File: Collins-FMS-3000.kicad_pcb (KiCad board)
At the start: 2 copper layers, 145 x 161 mm, 142 parts, among them J1 USB_B_Mini, J2 AVR-ISP-6, J3 Conn_02x04_Odd_Even, SW1 SW_Push_LED, SW10 SW_Push_LED, SW11 SW_Push_LED, SW12 SW_Push_LED, SW13 SW_Push_LED, SW14 SW_Push_LED, SW15 SW_Push_LED, SW16 SW_Push_LED, SW17 SW_Push_LED, SW18 SW_Push_LED, SW19 SW_Push_LED, SW2 SW_Push_LED, SW20 SW_Push_LED, SW21 SW_Push_LED, SW22 SW_Push_LED, SW23 SW_Push_LED, SW24 SW_Push_LED, SW25 SW_Push_LED, SW26 SW_Push_LED, SW27 SW_Push_LED, SW28 SW_Push_LED, SW29 SW_Push_LED, SW3 SW_Push_LED, SW30 SW_Push_LED, SW31 SW_Push_LED, SW32 SW_Push_LED, SW33 SW_Push_LED, SW34 SW_Push_LED, SW35 SW_Push_LED, SW36 SW_Push_LED, SW37 SW_Push_LED, SW38 SW_Push_LED, SW39 SW_Push_LED, SW4 SW_Push_LED, SW40 SW_Push_LED, SW41 SW_Push_LED, SW42 SW_Push_LED, SW43 SW_Push_LED, SW44 SW_Push_LED, SW45 SW_Push_LED, SW46 SW_Push_LED, SW47 SW_Push_LED, SW48 SW_Push_LED, SW49 SW_Push_LED, SW5 SW_Push_LED, SW50 SW_Push_LED, SW51 SW_Push_LED, SW52 SW_Push_LED, SW53 SW_Push_LED, SW54 SW_Push_LED, SW55 SW_Push_LED, SW56 SW_Push_LED, SW57 SW_Push_LED, SW58 SW_Push_LED, SW59 SW_Push_LED, SW6 SW_Push_LED, SW60 SW_Push_LED, SW61 SW_Push_LED, SW62 SW_Push_LED, SW63 SW_Push_LED, SW64 SW_Push_LED, SW65 SW_Push_LED, SW66 SW_Push_LED, SW67 SW_Push_LED, SW68 SW_Push_LED, SW69 SW_Push_LED, SW7 SW_Push_LED, SW8 SW_Push_LED, SW9 SW_Push_LED, U1 ATmega32U4-MU, U2 MCP23017_SO, U3 MCP23017_SO, U4 IS31FL3733B, Y1 16MHz

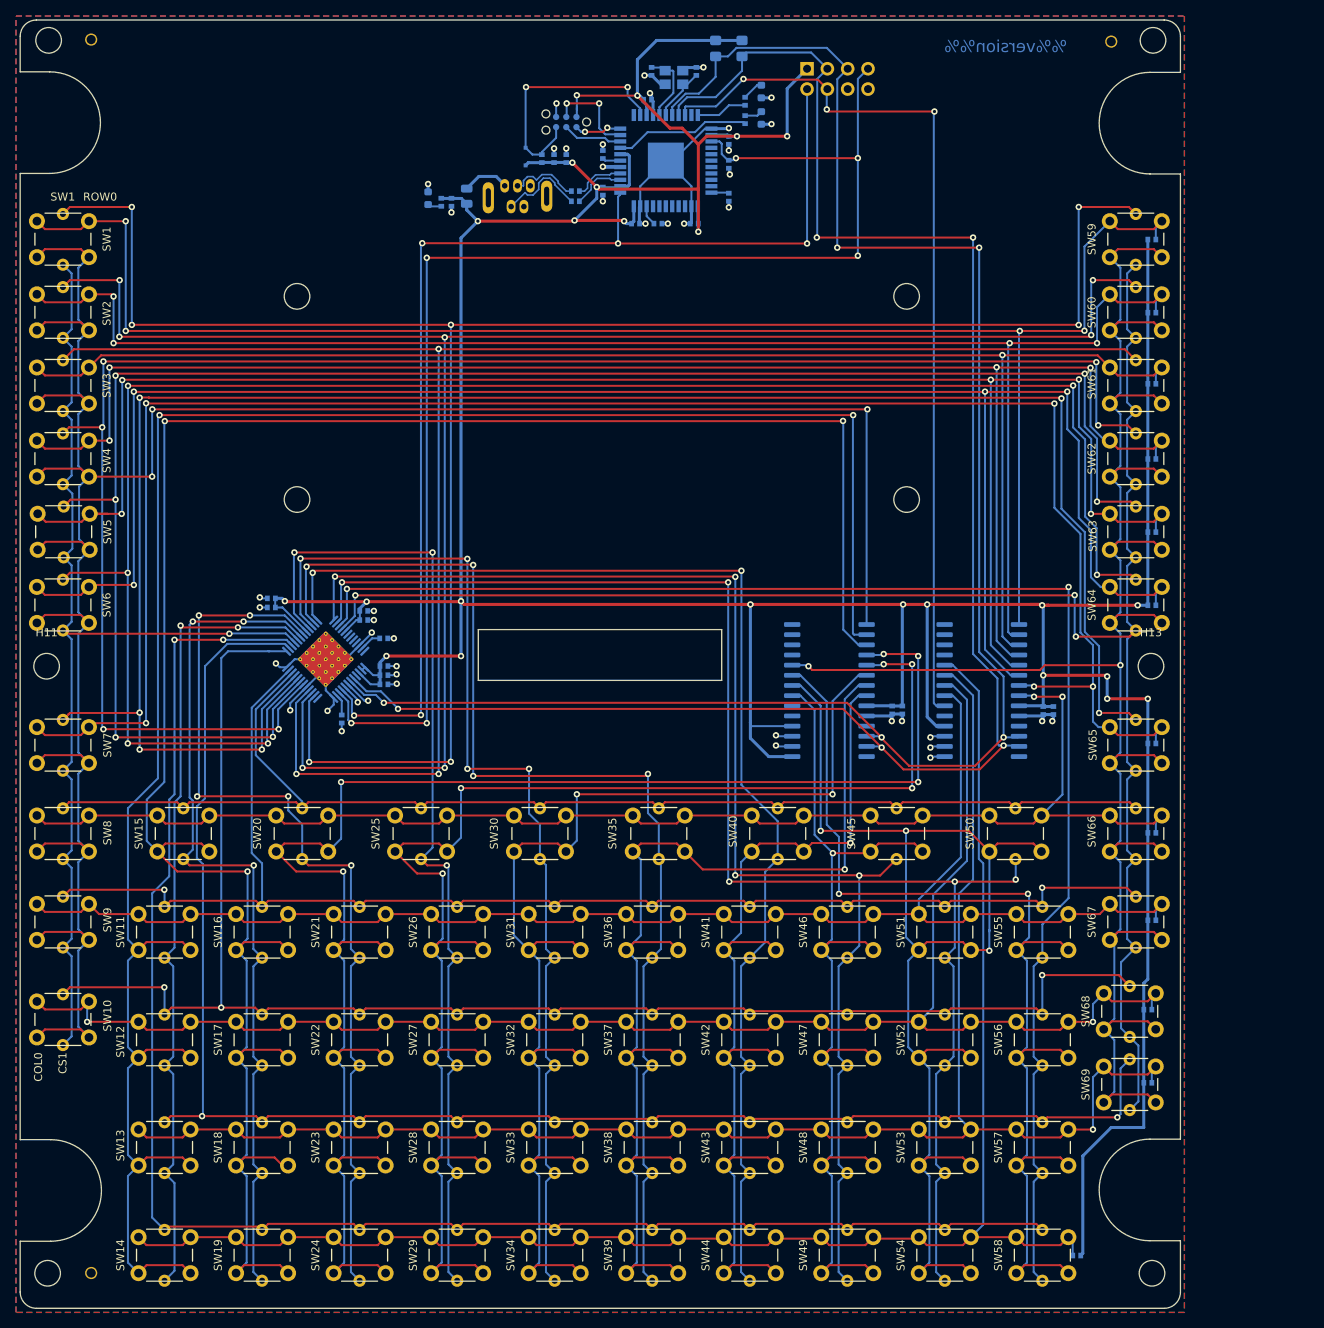
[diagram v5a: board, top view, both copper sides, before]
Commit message: Update components to match JLCPCB availability
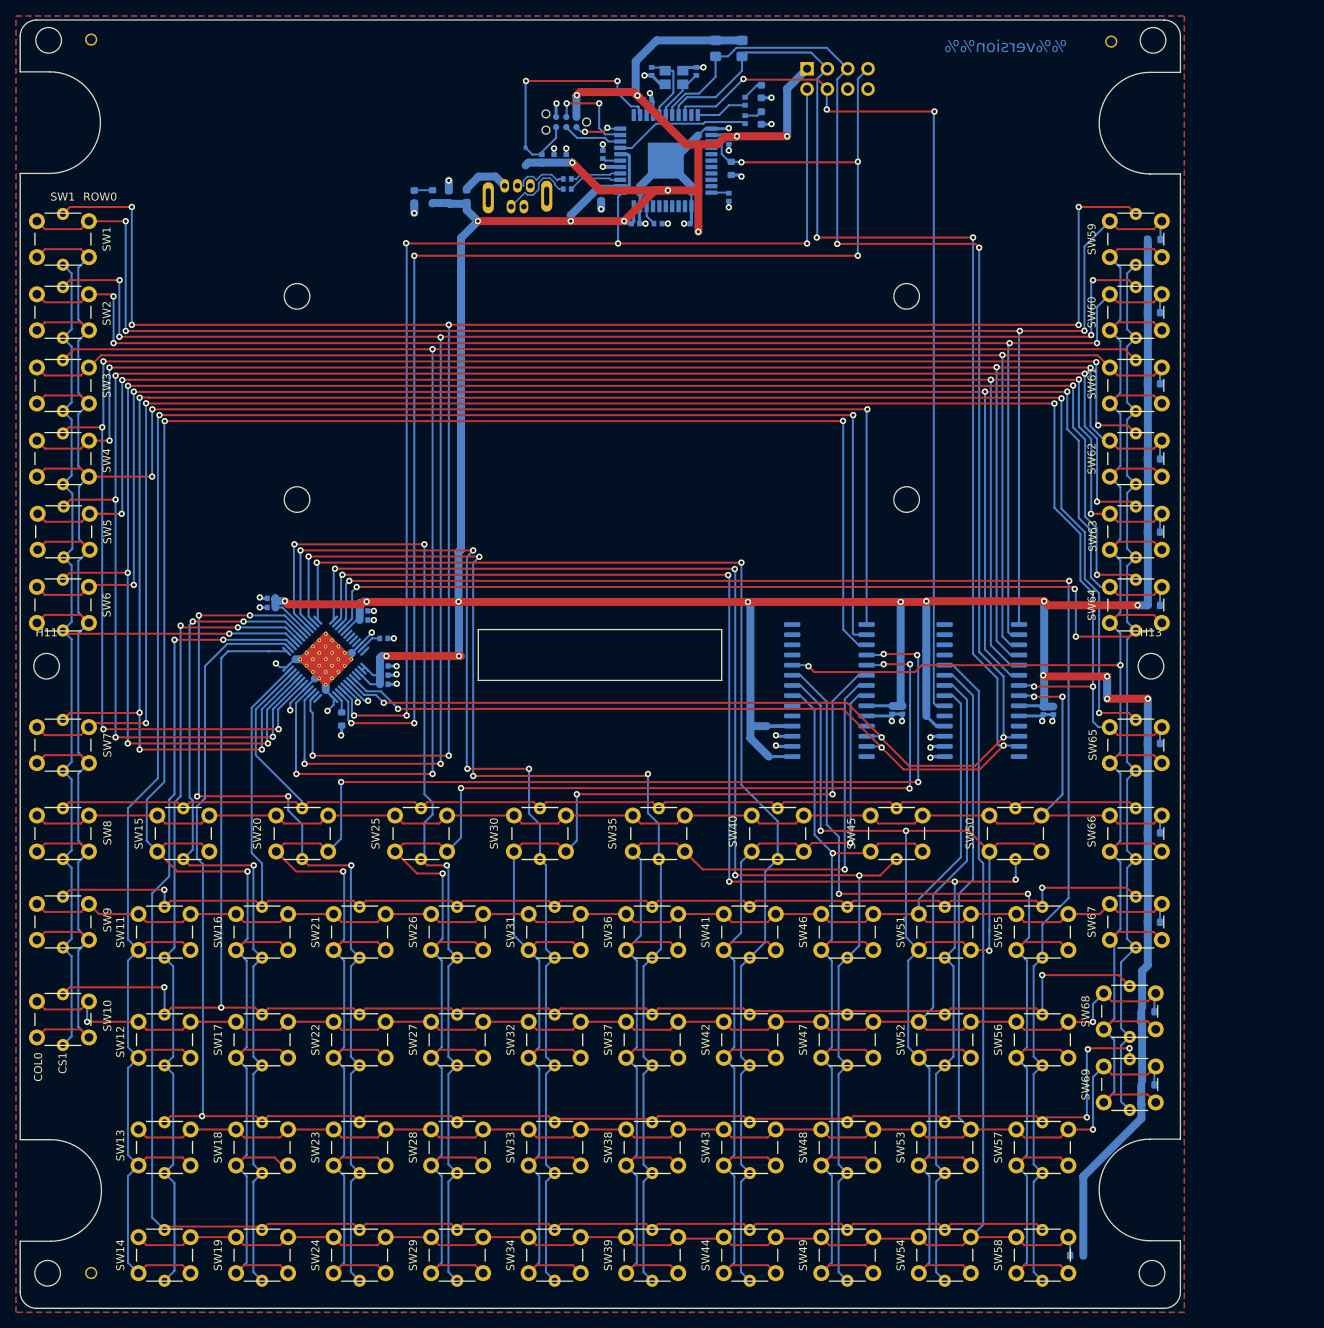
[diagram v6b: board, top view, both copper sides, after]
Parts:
- C10, C18: footprint Collins-FMS-3000:Perfect_0402 -> Capacitor_SMD:C_0603_1608Metric
- FB1: footprint Capacitor_SMD:C_0805_2012Metric -> Capacitor_SMD:C_0603_1608Metric
- R10, R11, R12, R13, R14, R15, R16, R17, R18, R19, R28, R3, R7, R8, R9: footprint Collins-FMS-3000:Perfect_0402 -> Resistor_SMD:R_0603_1608Metric
- moved R24 1.83 mm to (84.6, 36.1)
- moved R25 1.83 mm to (84.6, 37.4)
- moved D73 1.74 mm to (65.5, 38.4), turned to 90 degrees
- moved R28 1.29 mm to (67.7, 38.4), turned to 90 degrees
- moved C18 0.76 mm to (69.8, 38.4), turned to 90 degrees
- moved R3 0.60 mm to (105.1, 34.8)
- moved C10 0.51 mm to (88.8, 38.1)
- moved R16 0.32 mm to (157.8, 129.0)
- moved R8 0.26 mm to (157.9, 43.7)
- moved R17 0.25 mm to (157.1, 140.2)
- moved R18 0.25 mm to (157.1, 149.4)
- moved R10 0.19 mm to (157.8, 61.7)
- moved R11 0.19 mm to (157.8, 71.1)
- moved R12 0.19 mm to (157.8, 80.3)
- moved R13 0.19 mm to (157.8, 89.4)
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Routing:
- net +5V: track 561.9 -> 727.0 mm
- net GND: track 121.1 -> 138.7 mm
- net /LEDMatrix/SW11: track 201.4 -> 204.9 mm, vias 2 -> 4
- net /LEDMatrix/CS6: track 131.9 -> 135.0 mm
- net /LEDMatrix/CS7: track 144.0 -> 146.8 mm
- net /LEDMatrix/SW1: track 245.3 -> 243.2 mm
- net /LEDMatrix/CS9: track 168.3 -> 170.2 mm
- net /LEDMatrix/CS10: track 182.7 -> 184.5 mm
- net /LEDMatrix/CS12: track 222.8 -> 224.6 mm
- net /LEDMatrix/SW2: track 230.3 -> 228.5 mm
- net /ATmega32u4/DR-: track 11.0 -> 9.42 mm
- net /LEDMatrix/CS11: track 186.1 -> 187.7 mm
- net /ATmega32u4/DR+: track 9.03 -> 7.43 mm
- net /LEDMatrix/CS5: track 125.2 -> 126.7 mm
- net /LEDMatrix/CS8: track 154.7 -> 156.1 mm
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
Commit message: Add via stitching
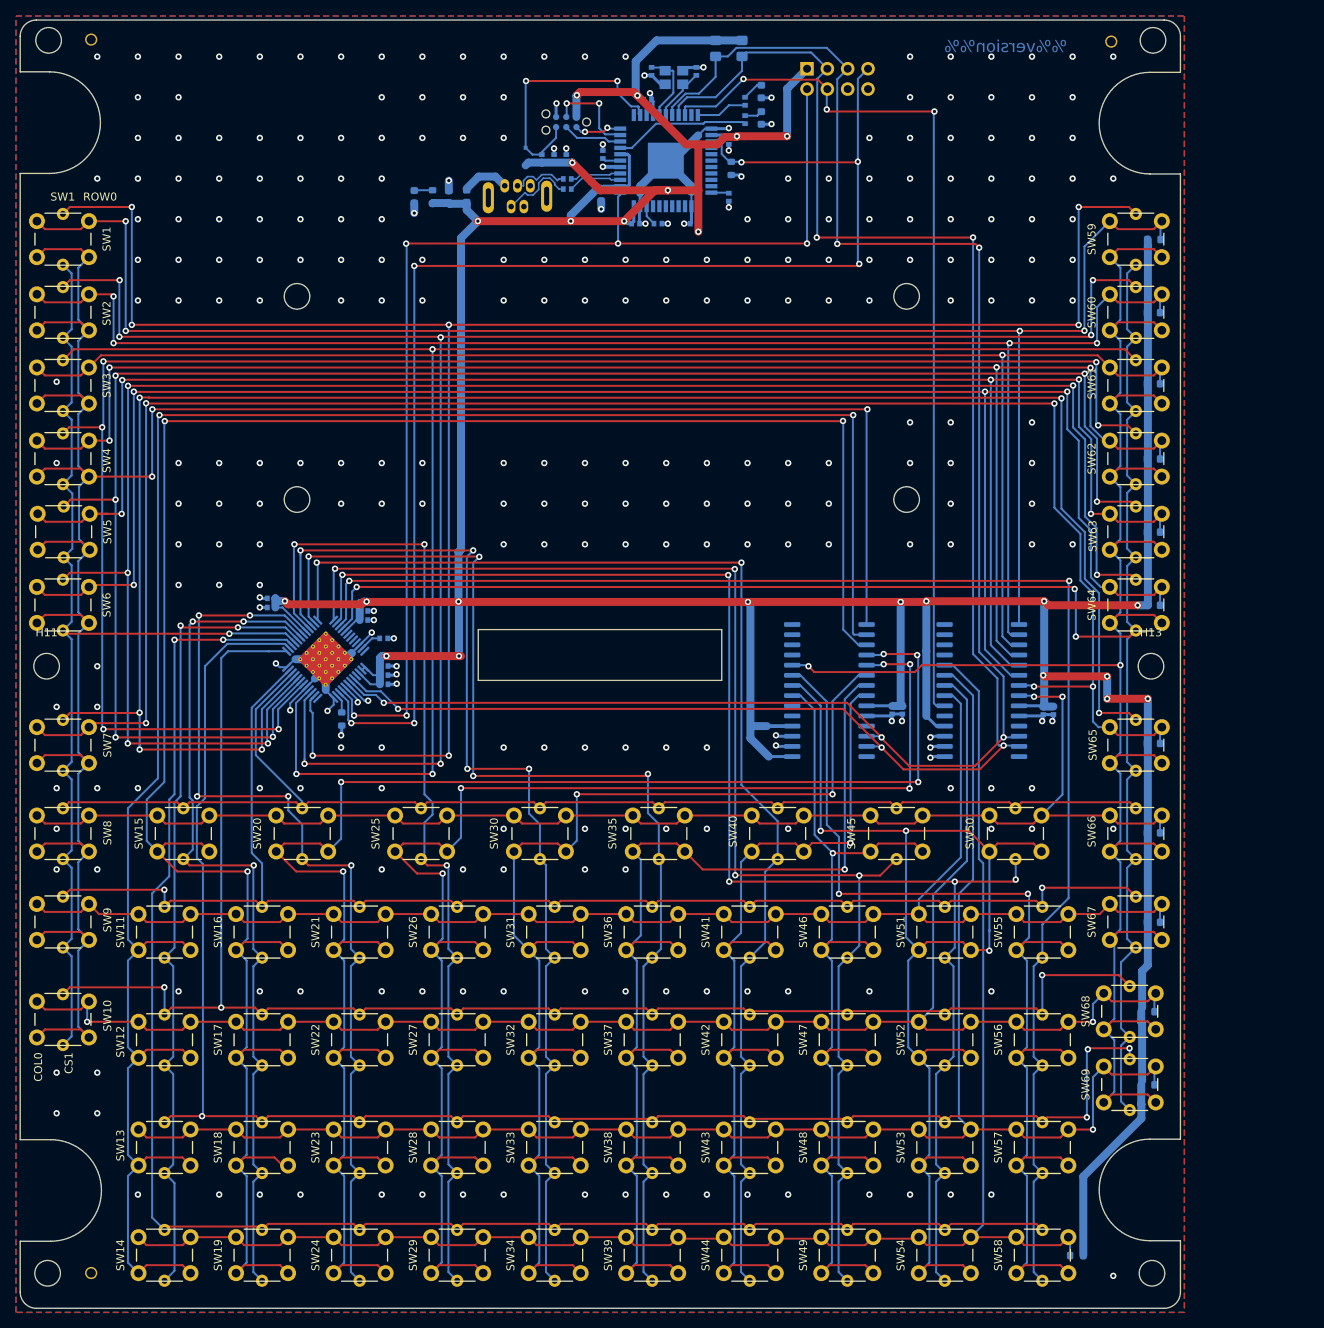
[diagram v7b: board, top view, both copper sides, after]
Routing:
- net GND: vias 44 -> 303

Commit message: Switch to keystone test points
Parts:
- removed J3: Conn_02x04_Odd_Even, Connector_PinHeader_2.54mm:PinHeader_2x04_P2.54mm_Vertical
- added TP1: TestPoint, TestPoint:TestPoint_Keystone_5005-5009_Compact, F.Cu at (119.8, 23.4)
- added TP2: TestPoint, TestPoint:TestPoint_Keystone_5005-5009_Compact, F.Cu at (124.9, 23.4)
- added TP3: TestPoint, TestPoint:TestPoint_Keystone_5005-5009_Compact, F.Cu at (130.0, 23.4)
- added TP4: TestPoint, TestPoint:TestPoint_Keystone_5005-5009_Compact, F.Cu at (114.7, 23.4)
- added TP5: TestPoint, TestPoint:TestPoint_Keystone_5005-5009_Compact, F.Cu at (135.1, 23.4)
- added TP6: TestPoint, TestPoint:TestPoint_Keystone_5005-5009_Compact, F.Cu at (140.1, 23.4)
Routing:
- net SDB: track 170.3 -> 186.4 mm, vias 6 -> 7
- net +5V: track 727.0 -> 711.2 mm, vias 24 -> 23
- net ROW_INTA: track 112.4 -> 122.0 mm, vias 3 -> 2
- net I2C_SDA: track 222.1 -> 219.7 mm
- net I2C_SCL: track 222.9 -> 220.5 mm
- net LED_INTB: track 145.3 -> 146.9 mm
- net GND: vias 303 -> 290
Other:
- board text removed: "+5V"
